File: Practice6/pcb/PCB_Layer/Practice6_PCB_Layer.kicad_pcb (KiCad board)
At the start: 2 copper layers, 61.5 x 42.5 mm, 19 parts, among them J1 Conn_01x03, SW1 SW_1, SW2 SW_2, SW3 SW_3, SW4 SW_4, SW5 SW_5, SW6 SW_6, U1 ProMicro

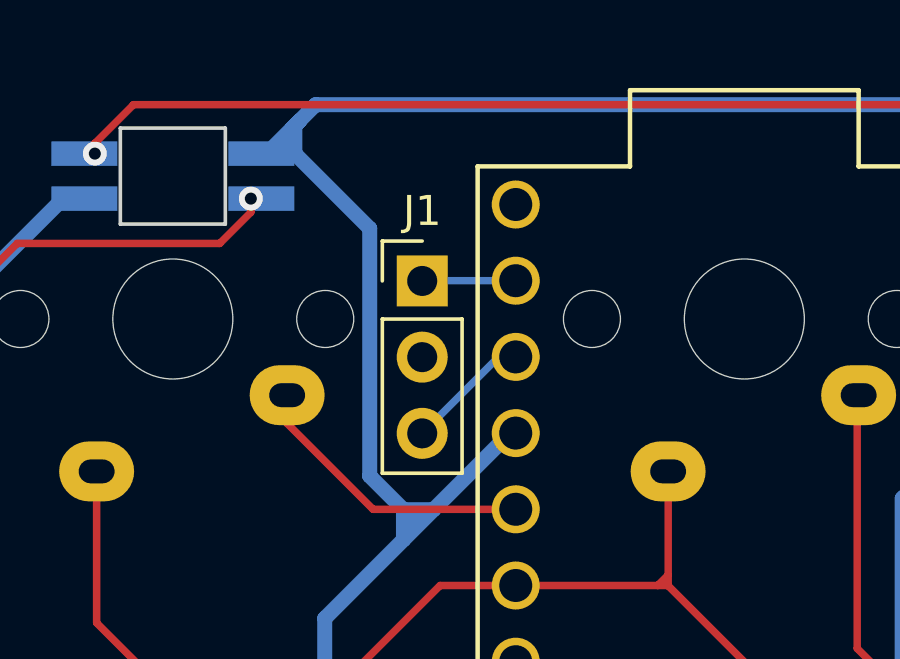
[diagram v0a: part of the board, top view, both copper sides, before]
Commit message: fix: RST switch parts, hole position
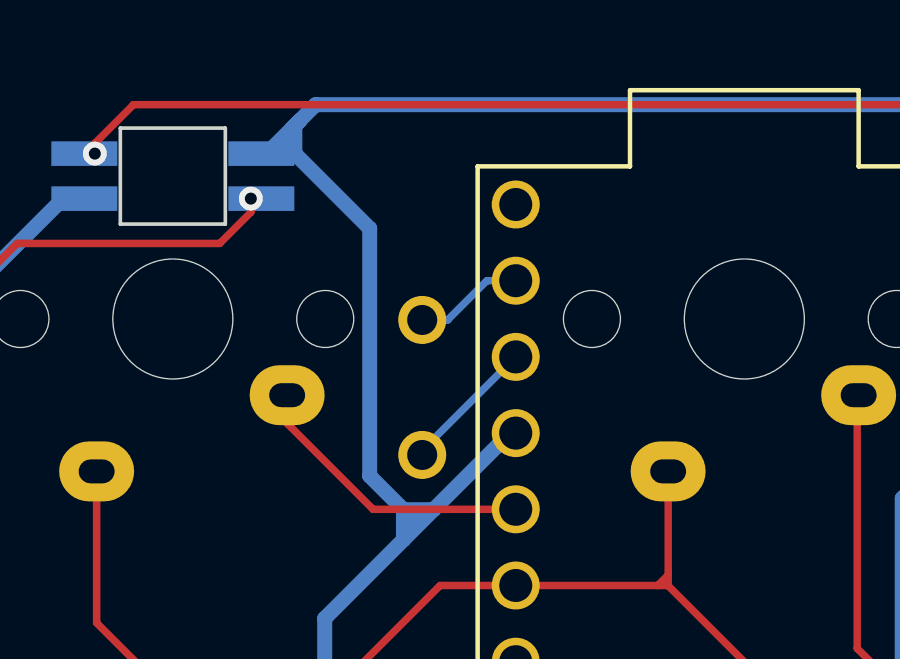
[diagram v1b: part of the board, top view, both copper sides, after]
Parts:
- J1: value Conn_01x03 -> Conn_01x02; footprint Connector_PinHeader_2.54mm:PinHeader_1x03_P2.54mm_Vertical -> akizukidenshi_parts:SW_108077_THDP07-060CB; moved to B.Cu
- moved J1 3.55 mm to (175.0, 99.8), turned to -90 degrees
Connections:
- J1 pad 1: Net-(U1-Pad23) -> RST
- J1 pad 2: unconnected-(J1-Pad2) -> RST_GND
- U1 pad 22: Net-(U1-Pad22) -> RST
- U1 pad 23: Net-(U1-Pad23) -> RST_GND
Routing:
- net RST: track 0.00 -> 4.58 mm
- net Net-(U1-Pad22): track 4.20 -> 0.00 mm
- net RST_GND: track 0.00 -> 3.66 mm
- net Net-(U1-Pad23): track 3.12 -> 0.00 mm
